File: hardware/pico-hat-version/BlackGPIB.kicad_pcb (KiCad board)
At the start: 2 copper layers, 119.1 x 55 mm, 5 parts, among them J1 SD_Card_Module, J2 Raspberry_Pi_Connector

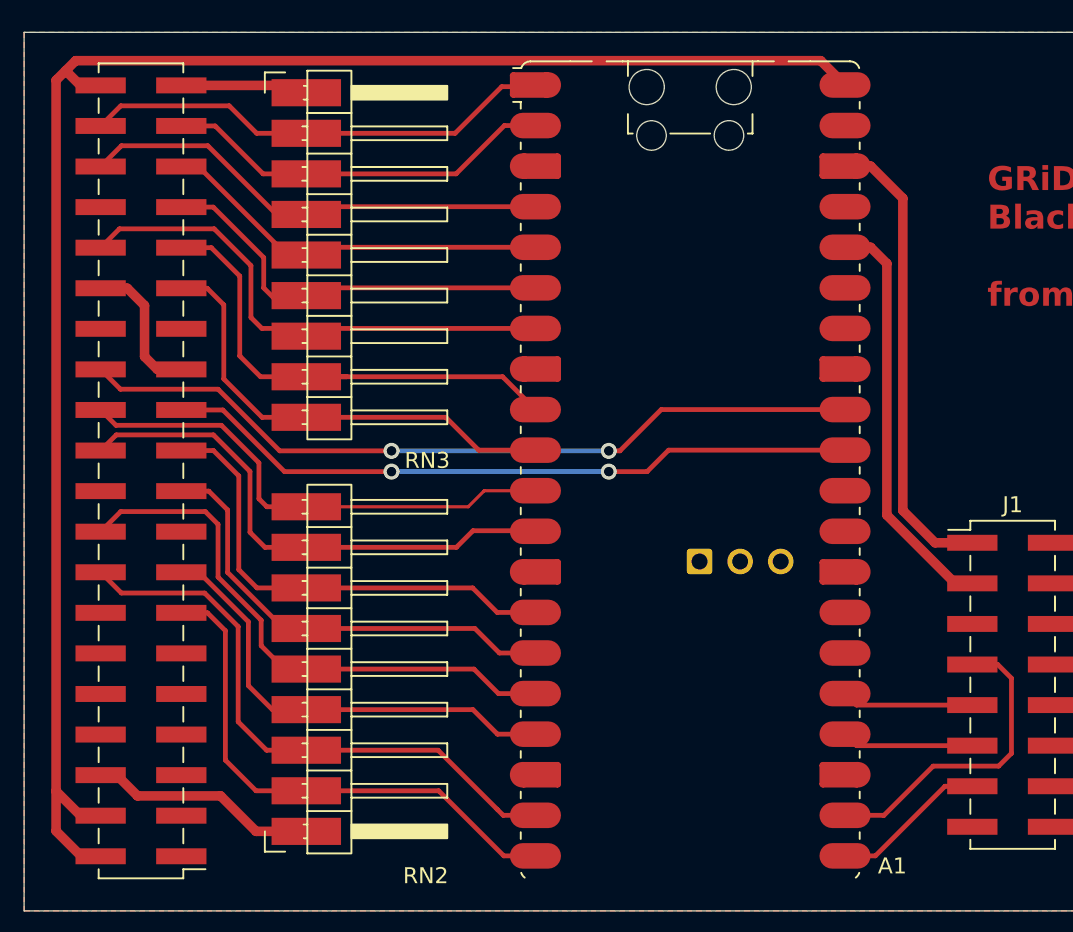
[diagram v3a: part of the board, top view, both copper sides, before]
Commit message: pico: move DC TE traces in hatted version to make handicraft easier
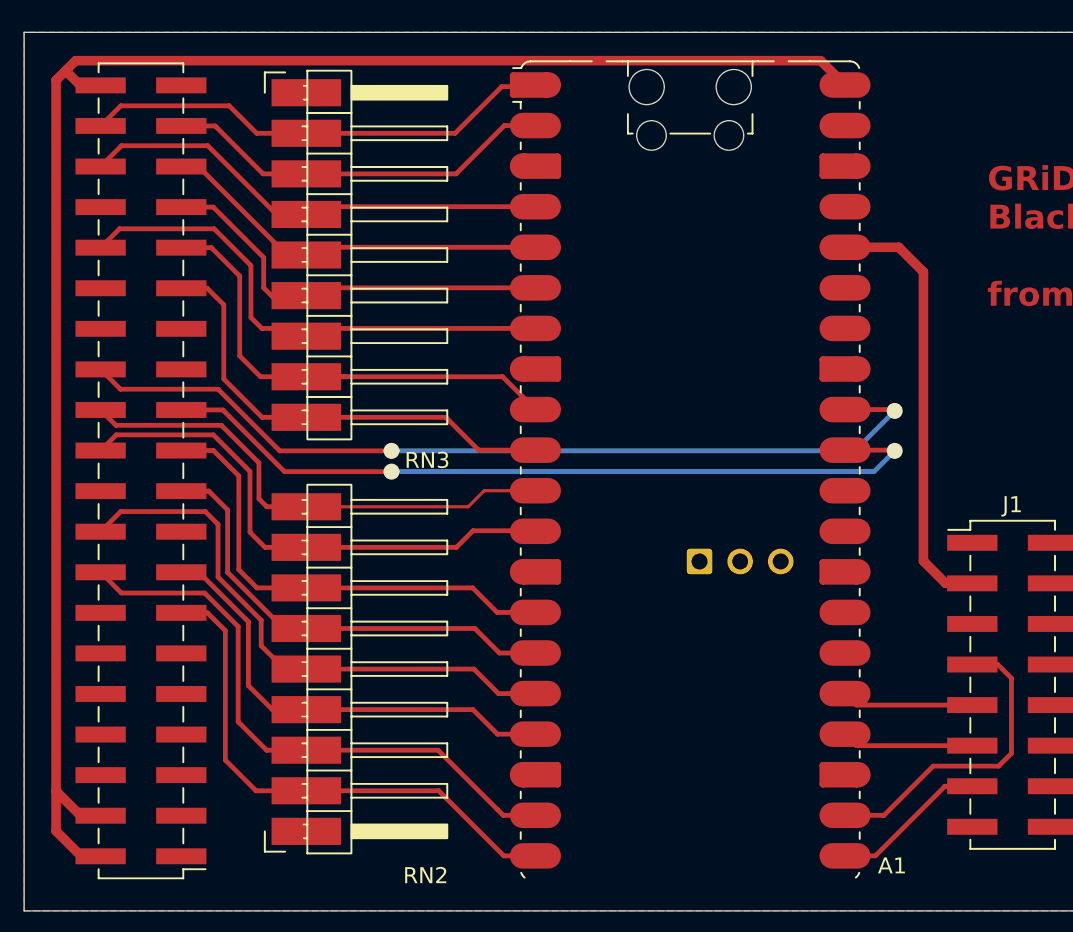
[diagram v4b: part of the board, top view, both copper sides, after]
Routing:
- net GND: track 58.8 -> 0.85 mm
- net GPIB_TE: track 49.8 -> 56.0 mm
- net GPIB_DC: track 43.7 -> 49.9 mm
- net +3.3V: track 25.9 -> 27.3 mm
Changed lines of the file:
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@@
+	)
+	(segment
+		(start 169.115 77.415)
+		(end 166.09 77.415)
+		(width 0.3)
+		(layer "F.Cu")
+		(net 2)
 	)
 	(segment
@@
 	)
 	(segment
-		(start 152 80)
-		(end 151.3 80)
-		(width 0.3)
-		(layer "F.Cu")
-		(net 2)
-	)
-	(segment
 		(start 137.7 80)
 		(end 130.7 80)
@@
 	)
 	(segment
-		(start 166.09 77.415)
-		(end 154.585 77.415)
-		(width 0.3)
-		(layer "F.Cu")
-		(net 2)
-	)
-	(segment
-		(start 154.585 77.415)
-		(end 152 80)
+		(start 169.2 77.5)
+		(end 169.115 77.415)
 		(width 0.3)
 		(layer "F.Cu")
@@
 	)
 	(via
-		(at 151.3 80)
+		(at 169.2 77.5)
 		(size 1)
-		(drill 0.6)
+		(drill 0.001)
 		(layers "F.Cu" "B.Cu")
 		(net 2)
@@
 		(at 137.7 80)
 		(size 1)
-		(drill 0.6)
+		(drill 0.001)
 		(layers "F.Cu" "B.Cu")
 		(net 2)
 	)
 	(segment
-		(start 151.3 80)
+		(start 169.2 77.5)
+		(end 166.7 80)
+		(width 0.3)
+		(layer "B.Cu")
+		(net 2)
+	)
+	(segment
+		(start 166.7 80)
 		(end 137.7 80)
 		(width 0.3)
 		(layer "B.Cu")
 		(net 2)
-	)
-	(segment
-		(start 124.54 74.9)
-		(end 123.04 74.9)
-		(width 0.6)
-		(layer "F.Cu")
-		(net 3)
-	)
-	(segment
-		(start 131.04 57.58)
-		(end 130.58 57.12)
-		(width 0.2)
-		(layer "F.Cu")
-		(net 3)
-	)
-	(segment
-		(start 121.16 69.82)
-		(end 119.49 69.82)
-		(width 0.6)
-		(layer "F.Cu")
-		(net 3)
-	)
-	(segment
-		(start 131.04 103.82)
-		(end 129.22 103.82)
-		(width 0.6)
-		(layer "F.Cu")
-		(net 3)
-	)
-	(segment
-		(start 122.24 70.9)
-		(end 121.16 69.82)
-		(width 0.6)
-		(layer "F.Cu")
-		(net 3)
-	)
-	(segment
-		(start 127 101.6)
-		(end 121.8 101.6)
-		(width 0.6)
-		(layer "F.Cu")
-		(net 3)
-	)
-	(segment
-		(start 130.58 57.12)
-		(end 124.54 57.12)
-		(width 0.6)
-		(layer "F.Cu")
-		(net 3)
-	)
-	(segment
-		(start 120.5 100.3)
-		(end 119.49 100.3)
-		(width 0.6)
-		(layer "F.Cu")
-		(net 3)
-	)
-	(segment
-		(start 169.71 83.735)
-		(end 169.71 64.19)
-		(width 0.6)
-		(layer "F.Cu")
-		(net 3)
-	)
-	(segment
-		(start 123.04 74.9)
-		(end 122.24 74.1)
-		(width 0.6)
-		(layer "F.Cu")
-		(net 3)
-	)
-	(segment
-		(start 169.71 64.19)
-		(end 167.695 62.175)
-		(width 0.6)
-		(layer "F.Cu")
-		(net 3)
-	)
-	(segment
-		(start 122.24 74.1)
-		(end 122.24 70.9)
-		(width 0.6)
-		(layer "F.Cu")
-		(net 3)
-	)
-	(segment
-		(start 129.22 103.82)
-		(end 127 101.6)
-		(width 0.6)
-		(layer "F.Cu")
-		(net 3)
-	)
-	(segment
-		(start 174.06 85.755)
-		(end 171.73 85.755)
-		(width 0.6)
-		(layer "F.Cu")
-		(net 3)
-	)
-	(segment
-		(start 167.695 62.175)
-		(end 166.09 62.175)
-		(width 0.6)
-		(layer "F.Cu")
-		(net 3)
-	)
-	(segment
-		(start 121.8 101.6)
-		(end 120.5 100.3)
-		(width 0.6)
-		(layer "F.Cu")
-		(net 3)
-	)
-	(segment
-		(start 171.73 85.755)
-		(end 169.71 83.735)
-		(width 0.6)
-		(layer "F.Cu")
-		(net 3)
 	)
 	(segment
@@
 	)
 	(segment
-		(start 172.985 88.295)
-		(end 168.71 84.02)
+		(start 172.395 88.295)
+		(end 171 86.9)
 		(width 0.6)
 		(layer "F.Cu")
@@
 	)
 	(segment
-		(start 168.71 84.02)
-		(end 168.71 68.275)
+		(start 171 68.8)
+		(end 169.455 67.255)
 		(width 0.6)
 		(layer "F.Cu")
@@
 	)
 	(segment
-		(start 168.71 68.275)
-		(end 167.69 67.255)
+		(start 169.455 67.255)
+		(end 166.09 67.255)
 		(width 0.6)
 		(layer "F.Cu")
@@
 	)
 	(segment
+		(start 171 86.9)
+		(end 171 68.8)
+		(width 0.6)
+		(layer "F.Cu")
+		(net 4)
+	)
+	(segment
 		(start 174.06 88.295)
-		(end 172.985 88.295)
-		(width 0.6)
-		(layer "F.Cu")
-		(net 4)
-	)
-	(segment
-		(start 167.69 67.255)
-		(end 166.09 67.255)
+		(end 172.395 88.295)
 		(width 0.6)
 		(layer "F.Cu")
@@
 	)
 	(segment
-		(start 166.09 79.955)
-		(end 155.045 79.955)
-		(width 0.3)
-		(layer "F.Cu")
-		(net 17)
-	)
-	(segment
 		(start 137.7 81.3)
 		(end 131 81.3)
@@
 	)
 	(segment
-		(start 153.7 81.3)
-		(end 151.3 81.3)
-		(width 0.3)
-		(layer "F.Cu")
-		(net 17)
-	)
-	(segment
-		(start 155.045 79.955)
-		(end 153.7 81.3)
+		(start 169.155 79.955)
+		(end 166.09 79.955)
 		(width 0.3)
 		(layer "F.Cu")
@@
 		(start 127.14 77.44)
 		(end 124.54 77.44)
+		(width 0.3)
+		(layer "F.Cu")
+		(net 17)
+	)
+	(segment
+		(start 169.2 80)
+		(end 169.155 79.955)
 		(width 0.3)
 		(layer "F.Cu")
@@
 		(at 137.7 81.3)
 		(size 1)
-		(drill 0.6)
+		(drill 0.001)
 		(layers "F.Cu" "B.Cu")
 		(net 17)
 	)
 	(via
-		(at 151.3 81.3)
+		(at 169.2 80)
 		(size 1)
-		(drill 0.6)
+		(drill 0.001)
 		(layers "F.Cu" "B.Cu")
 		(net 17)
 	)
 	(segment
-		(start 151.3 81.3)
+		(start 169.2 80)
+		(end 167.9 81.3)
+		(width 0.3)
+		(layer "B.Cu")
+		(net 17)
+	)
+	(segment
+		(start 167.9 81.3)
 		(end 137.7 81.3)
 		(width 0.3)
